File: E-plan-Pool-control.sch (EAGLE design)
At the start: 16 parts

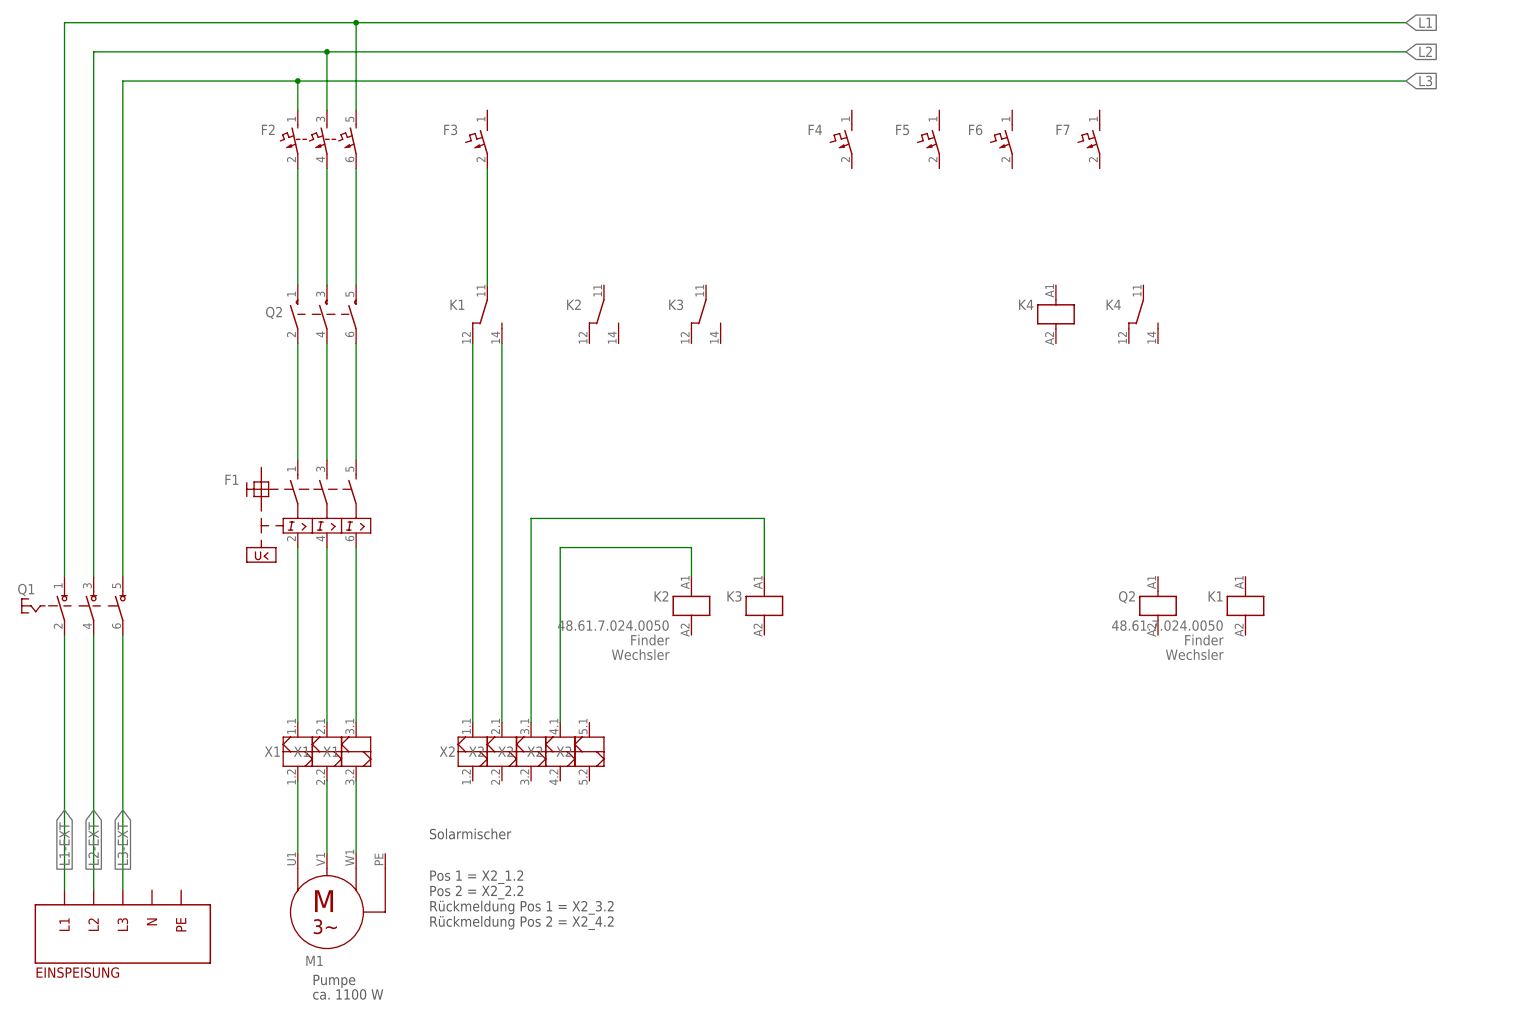
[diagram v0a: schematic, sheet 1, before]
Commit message: E-Plan-Pool added
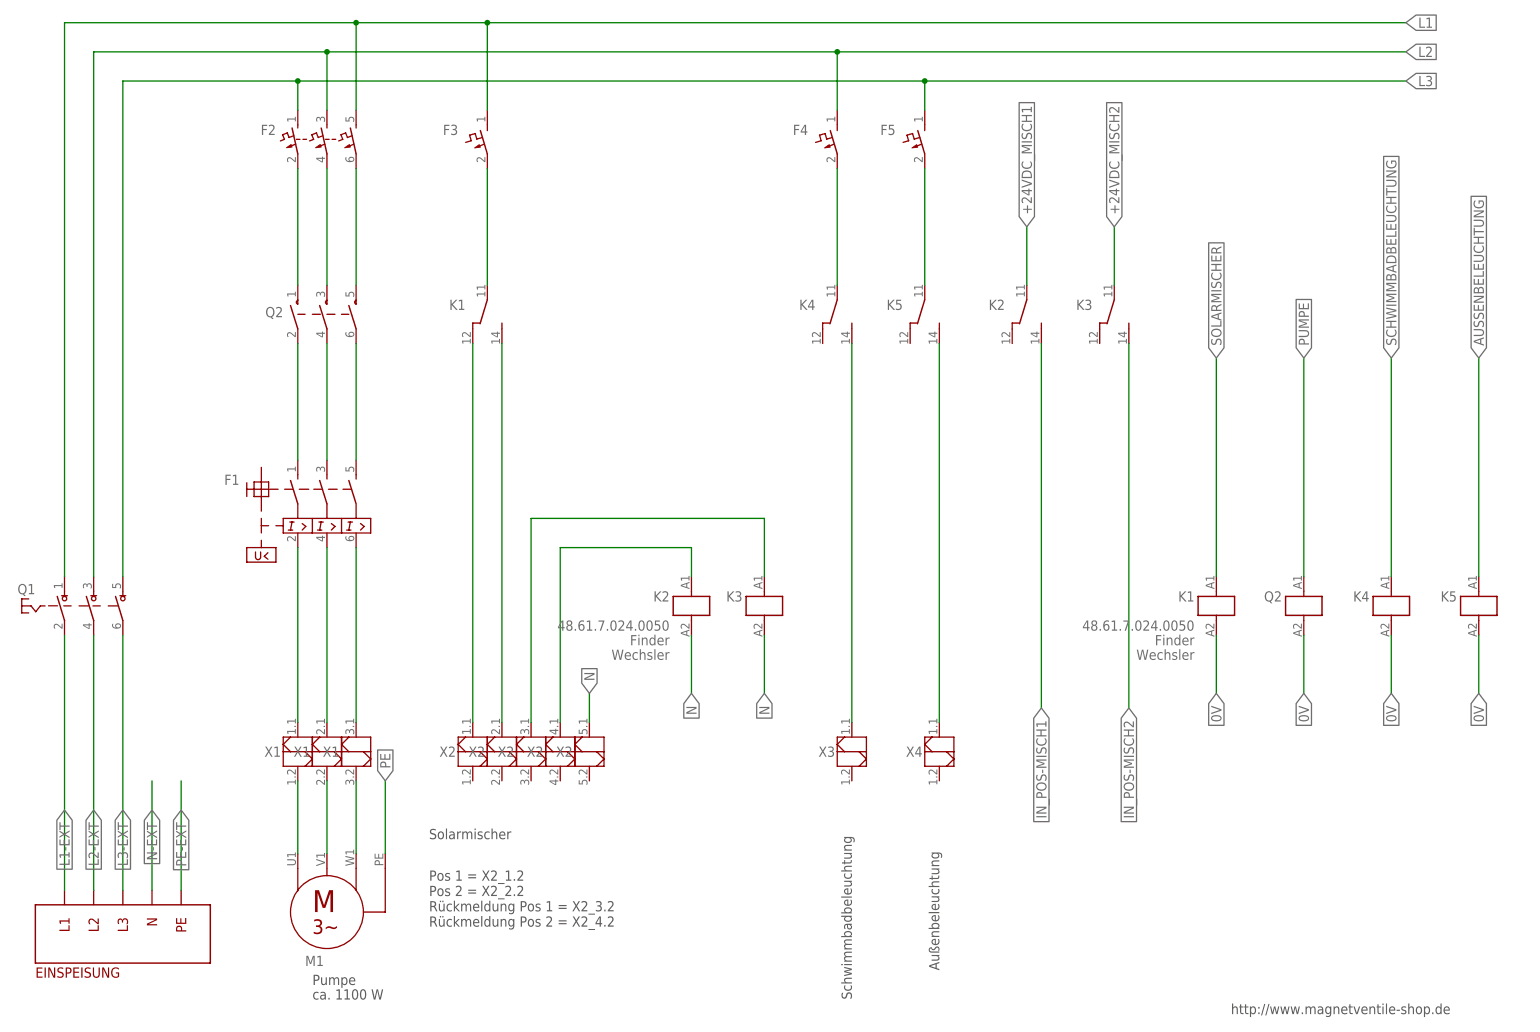
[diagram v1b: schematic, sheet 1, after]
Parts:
- added B1, B2, B3, B4, B5: (no value), e-messfuehler:MESSFUEHLER_2
- added EXT1: (no value), STRASYS_CONTRL:DIN-PT1000-EXT
- added F8: (no value), e-sicherungen:LEITUNGSSCHUTZSCHALTER
- added G1, G2: (no value), e-stromversorgungselemente:NETZTEIL_GLEICHSPANNUNG
- added K5: (no value), e-schuetze-relais:HILFSSCHUETZ_11-12-14
- added PLC1: (no value), STRASYS_CONTRL:DIN-RAIL-BASIS
- added X10, X6, X7, X8, X9: (no value), e-klemmen:KLEMME_2-2
- added X11: (no value), e-steckverbinder:STECKDOSE
- added X3, X4: (no value), e-klemmen:KLEMME-2_5-BRUECKE
- added X5: (no value), e-klemmen:KLEMME-2_4-BRUECKE
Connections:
- new net +24VDC: G2.4, X51.1
- new net +24VDC_DIGIOUT: PLC1.+24V, X51.2
- new net +24VDC_MISCH1: K21.1, X52.2
- new net +24VDC_MISCH2: K31.1, X53.2
- new net +24VDC_SCHWIMMERSCHALTER: X54.2, X6.1.2
- new net +5VDC: G1.4, PLC1.+5V
- new net 0V: G2.3, K10.A2, K40.A2, K50.A2, PLC1.0V, Q2G$1.A2
- new net AUSSENBELEUCHTUNG: K50.A1, PLC1.OUT4
- new net GND: G1.3, PLC1.GND
- new net IN_POS-MISCH1: K21.4, PLC1.IN2
- new net IN_POS-MISCH2: K31.4, PLC1.IN3
- new net N: G1.1, G2.1, K20.A2, K30.A2, X11.N, X25.1
- new net N$18: F4.2, K41.1
- new net N$19: K41.4, X31.1
- new net N$20: K51.4, X41.1
- new net N$21: F5.2, K51.1
- new net N$22: F6.2, G1.2
- new net N$23: F7.2, G2.2
- new net N$24: B5.1, X6.1.1
- new net N$25: F8.2, X11.L1
- new net N$26: B1.1, X7.1.1
- new net N$27: B5.2, X6.2.1
- new net N$28: B1.2, X7.2.1
- new net N$31: B2.1, X8.1.1
- new net N$32: B2.2, X8.2.1
- new net N$33: B3.1, X9.1.1
- new net N$34: B3.2, X9.2.1
- new net N$35: B4.1, X10.1.1
- new net N$36: B4.2, X10.2.1
- new net PE: M1.PE, X11.PE
- new net PT1000_AUSSEN: EXT1.PT1000_1, X7.1.2
- new net PT1000_BECKEN: EXT1.PT1000_4, X10.1.2
- new net PT1000_DACH: EXT1.PT1000_2, X8.1.2
- new net PT1000_GND: EXT1.PT_GND_1, EXT1.PT_GND_2, EXT1.PT_GND_3, EXT1.PT_GND_4, X10.2.2, X7.2.2, X8.2.2, X9.2.2
- new net PT1000_UMLAUF: EXT1.PT1000_3, X9.1.2
- new net PUMPE: PLC1.OUT2, Q2G$1.A1
- new net SCHWIMMBADBELEUCHTUNG: K40.A1, PLC1.OUT3
- new net SCHWIMMER: PLC1.IN1, X6.2.2
- new net SOLARMISCHER: K10.A1, PLC1.OUT1
- net L1: now also F3.1, F8.1
- net L2: now also F4.1, F7.1
- net L3: now also F5.1, F6.1
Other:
- note added: "Außenbeleuchtung"
- note added: "Schwimmbadbeleuchtung"
- note added: "http://www.magnetventile-shop.de"
- moved on the sheet: F4, F5, K1, K2, K3, K4, Q2
